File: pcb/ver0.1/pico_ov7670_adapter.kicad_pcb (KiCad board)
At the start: 2 copper layers, 53.2 x 70 mm, 21 parts, among them J1 GPIO Header, SW1 SW_Push, SW2 SW_Push, U1 CAMERA-OV7670, U2 RASPBERRY_PI_PICO_W

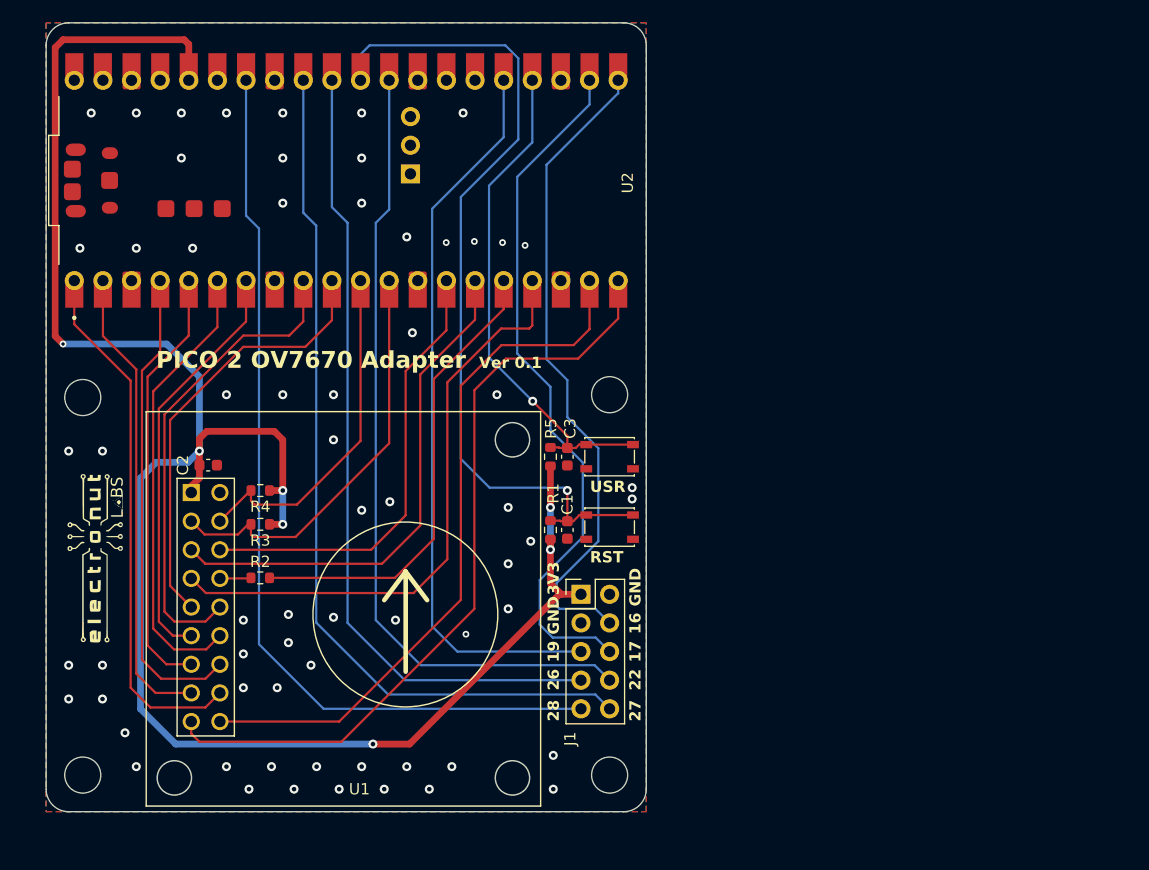
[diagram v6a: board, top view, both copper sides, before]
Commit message: updated layout changes as per the  feedback.
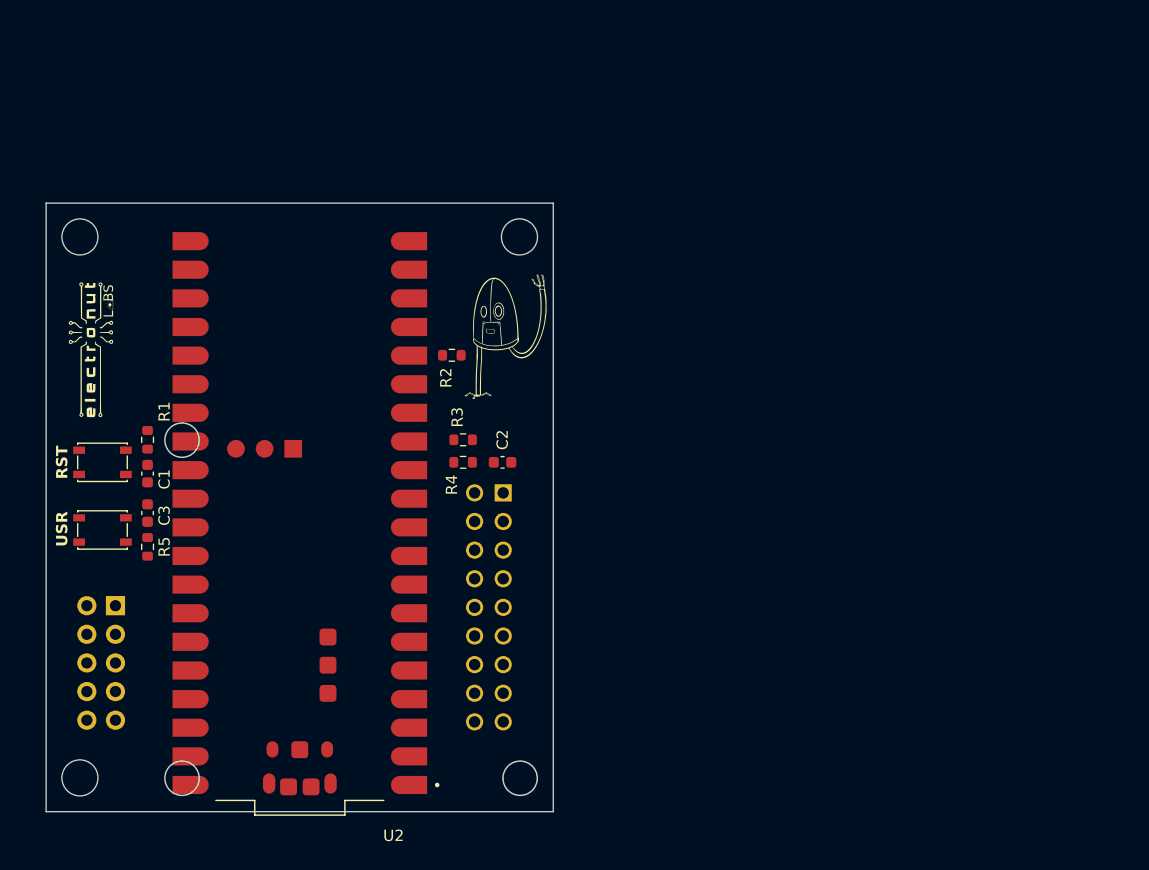
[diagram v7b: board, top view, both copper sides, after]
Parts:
- removed the G*** at (101.9, 65.5)
- removed H4: MountingHole, MountingHole:MountingHole_3.2mm_M3_DIN965
- G***: moved to F.Cu
- J1, U1: moved to B.Cu
- U2: value RASPBERRY_PI_PICO_W -> MODULE_RASPBERRY_PI_PICO_W; footprint pico_ov7670_adapter:MODULE_RASPBERRY_PI_PICO_W -> pico_ov7670_adapter:RASPBERRY_PI_PICO_W
- moved H2 67.0 mm to (93.0, 69.0)
- moved H1 58.0 mm to (93.0, 117.0)
- moved SW2 45.5 mm to (95.0, 95.0), turned to 180 degrees
- moved SW1 45.4 mm to (95.0, 89.0), turned to 180 degrees
- moved J1 41.3 mm to (96.2, 101.7), turned to 180 degrees
- moved H3 41.3 mm to (132.0, 69.0)
- moved C1 37.6 mm to (99.0, 90.0)
- moved C3 37.6 mm to (99.0, 93.5), turned to 90 degrees
- moved R1 36.6 mm to (99.0, 87.0), turned to -90 degrees
- moved R5 36.6 mm to (99.0, 96.5), turned to -90 degrees
- moved U2 29.8 mm to (112.5, 93.5), turned to 180 degrees
- moved G*** 28.1 mm to (112.5, 75.0)
- moved C2 26.1 mm to (130.5, 89.0), turned to 180 degrees
- moved R2 26.1 mm to (126.0, 79.5), turned to 180 degrees
- moved R3 19.5 mm to (127.0, 87.0)
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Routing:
- net +3V3: track 169.4 -> 0.00 mm, vias 7 -> 0
- net /PICO_IO28: track 81.5 -> 0.00 mm
- net /PICO_IO27: track 77.8 -> 0.00 mm
- net /PICO_RESET: track 75.6 -> 0.00 mm, vias 1 -> 0
- net /PICO_IO26: track 71.5 -> 0.00 mm
- net /PICO_IO22: track 71.4 -> 0.00 mm
- net OV_RST_PICO_IO14: track 68.4 -> 0.00 mm
- net /PICO_IO19: track 65.2 -> 0.00 mm
- net /PICO_IO17: track 62.1 -> 0.00 mm
- net OV_PWDWN_PICO_IO15: track 61.9 -> 0.00 mm
- net /PICO_IO16: track 58.1 -> 0.00 mm
- net OV_PCLK_PICO_IO9: track 53.0 -> 0.00 mm
- net OV_D0_PICO_IO0: track 47.4 -> 0.00 mm
- net OV_VSYNC_PICO_IO10: track 45.2 -> 0.00 mm
- net /USER_Button: track 44.5 -> 0.00 mm, vias 1 -> 0
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- removed copper zone on B.Cu, net GND
- removed copper zone on F.Cu, net GND
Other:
- board size 53.2 x 70 mm -> 45 x 54 mm

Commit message: layout updated.
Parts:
- added G***: LOGO, pico_ov7670_adapter:art1, F.Cu at (95.5, 79.5)
- added R6: 22R, Resistor_SMD:R_0603_1608Metric, F.Cu at (126.2, 77.0)
- G***: moved to B.Cu
- U2: value MODULE_RASPBERRY_PI_PICO_W -> RASPBERRY_PI_PICO_W
- moved G*** 8.31 mm to (97.0, 86.8)
- moved H1 0.35 mm to (93.2, 116.8)
- moved H2 0.35 mm to (93.2, 69.2)
- moved H3 0.35 mm to (131.8, 69.2)
- moved G*** 0.25 mm to (130.0, 78.8)
- moved U1 0.25 mm to (117.3, 102.0)
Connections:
- U2 pad 17: OV_PCLK_PICO_IO9 -> Net-(U2-UART0_RX/I2C0_SCL/SPI1_CSN/GP13)
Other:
- outline, holes or cut-outs redrawn
- board text added: "PICO 2 OV7670 Adapter 0.1"
- board text removed: "PICO 2 OV7670 Adapter"
- board text removed: "Ver 0.1"
